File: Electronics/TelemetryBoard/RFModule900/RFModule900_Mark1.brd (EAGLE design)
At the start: 100 x 80 mm, 82 parts, among them U1 TPS2561, U2 TPS2561, Y1 30 Mhz

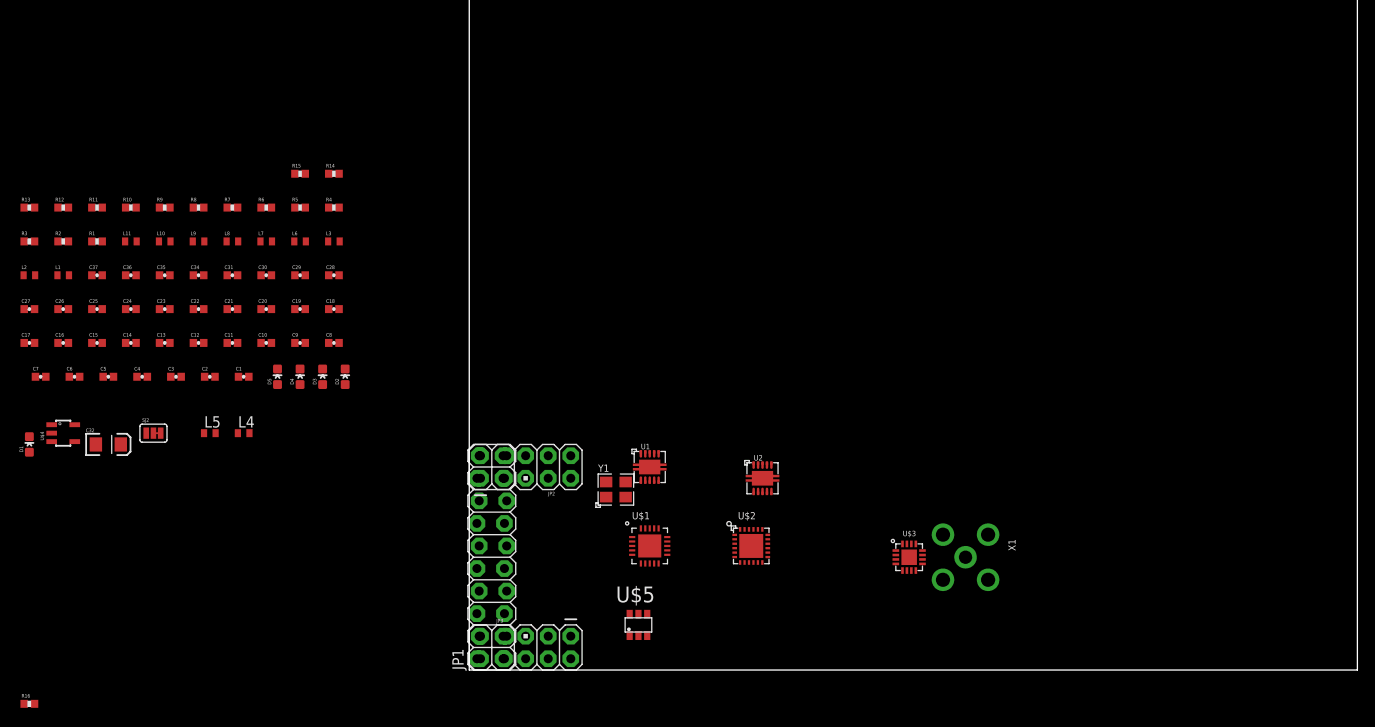
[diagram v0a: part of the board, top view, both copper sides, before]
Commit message: starting board routing
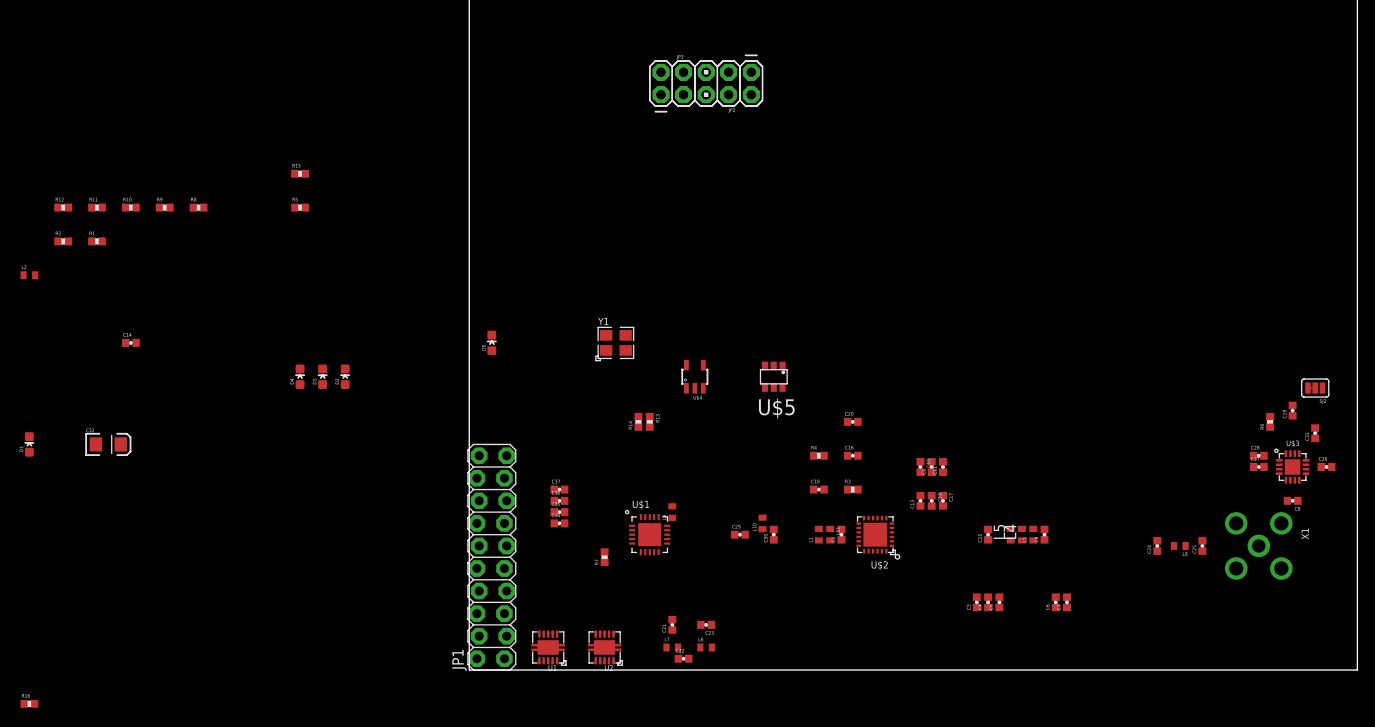
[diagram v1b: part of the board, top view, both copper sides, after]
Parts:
- moved C26 143.3 mm to (96.5, 22.9)
- moved C27 139.6 mm to (88.9, 22.9)
- moved SJ2 130.9 mm to (95.2, 31.8), turned to 180 degrees
- moved C25 127.3 mm to (82.5, 14.0), turned to 90 degrees
- moved C31 123.2 mm to (95.2, 26.7), turned to 90 degrees
- moved C24 118.6 mm to (77.5, 14.0), turned to 90 degrees
- moved C7 118.3 mm to (67.3, 7.62), turned to 90 degrees
- moved R6 115.6 mm to (90.2, 27.9), turned to 90 degrees
- moved C6 113.4 mm to (66.0, 7.62), turned to 90 degrees
- moved C19 112.3 mm to (92.7, 29.2), turned to 90 degrees
- moved L8 112.1 mm to (80.0, 14.0), turned to 180 degrees
- moved C8 109.4 mm to (92.7, 19.1), turned to 180 degrees
- moved C28 106.1 mm to (88.9, 24.1)
- moved C17 104.4 mm to (53.3, 19.1), turned to 270 degrees
- moved C5 103.5 mm to (59.7, 7.62), turned to 90 degrees
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
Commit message: More work on RF card
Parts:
- added C33: 0.01uF, SparkFun-Capacitors:0402-CAP
- C11, C15, C17: device SparkFun-Capacitors:0402-CAP -> SparkFun-Capacitors:EIA3216
- L4, L5: value (none) -> 260; device inductors:0402 -> SparkFun-Passives:0603
- moved L4 115.8 mm to (-49.5, -15.2), turned to 0 degrees
- moved L5 115.7 mm to (-49.5, -19.1), turned to 0 degrees
- moved C15 114.9 mm to (-47.0, -30.5), turned to 0 degrees
- moved C11 110.3 mm to (-47.0, -22.9), turned to 0 degrees
- moved C17 110.3 mm to (-47.0, -26.7), turned to 0 degrees
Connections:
- net GND: now also C11.C, C15.C, C17.C, C33.1; no longer C11.2, C15.2, C17.2
- net N$19: now also C11.A; no longer C11.1
- net N$3: now also C17.A; no longer C17.1
- net N$6: now also L4.2, L5.2; no longer L4.1, L5.1
- net PA_3V3: now also C15.A, C33.2, L4.1, L5.1; no longer C15.1, L4.2, L5.2

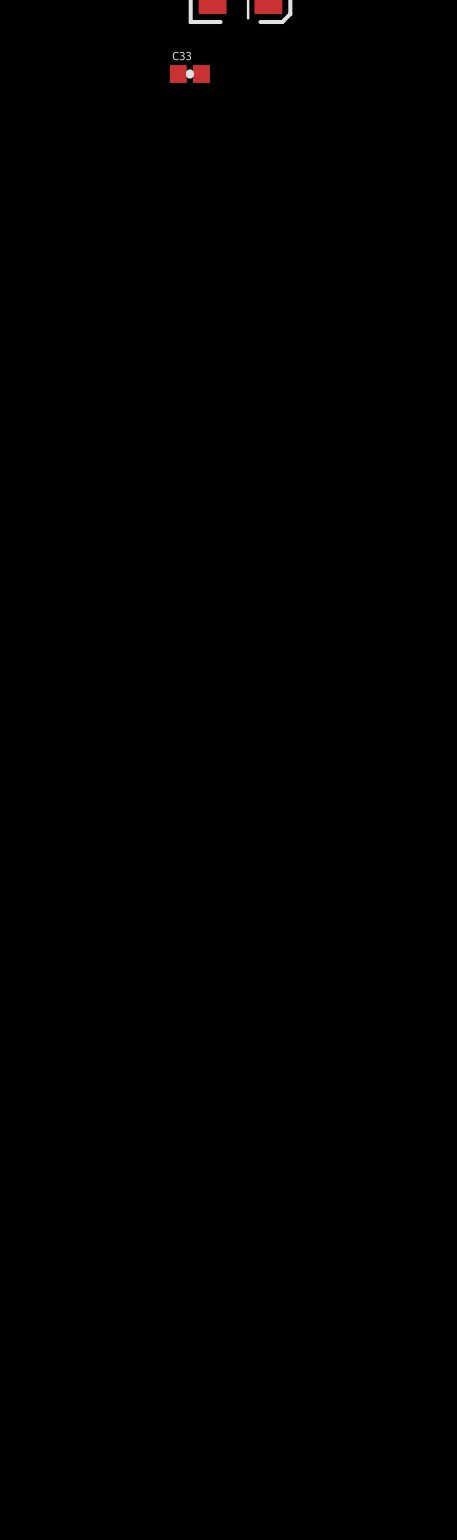
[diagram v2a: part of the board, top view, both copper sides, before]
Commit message: adding directional couplers to board
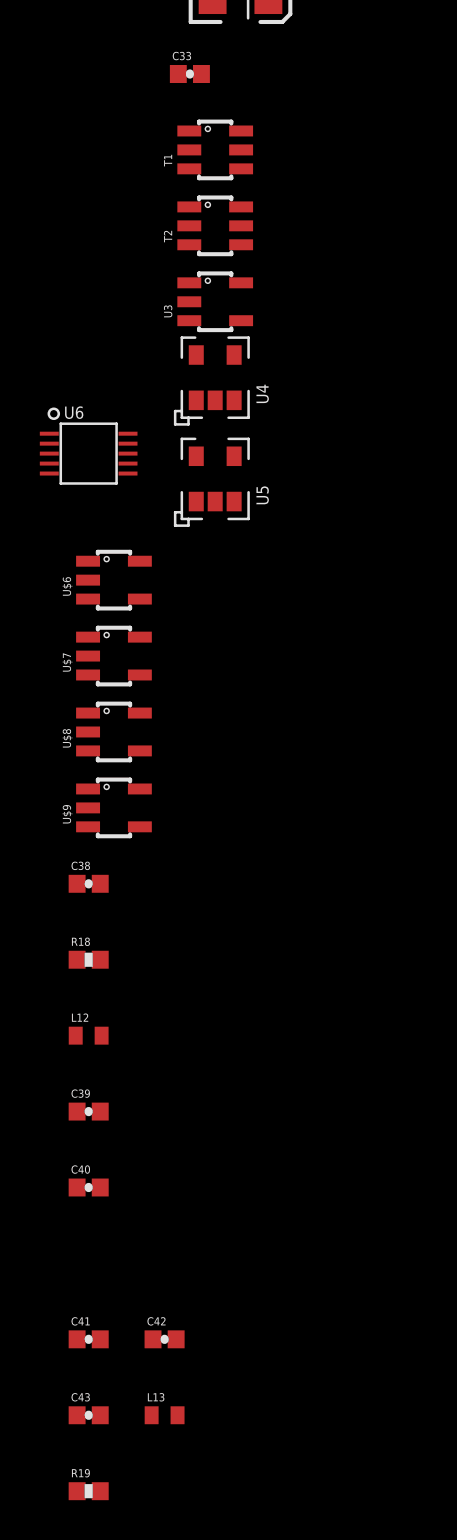
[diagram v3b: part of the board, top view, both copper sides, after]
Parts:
- added C38, C41: 0.1uF, SparkFun-Capacitors:0402-CAP
- added C39, C40, C42, C43: DNP, SparkFun-Capacitors:0402-CAP
- added L12, L13: 0 ohm, SparkFun-Passives:C0402
- added R18, R19: 5k, SparkFun-Resistors:0402-RES
- added T1, T2: DC08-73, RitLaunchInitiative:SOT23-6
- added U$6: TL331-Q1, RitLaunchInitiative:SOT23-5
- added U$7: SN74AHC1G08, RitLaunchInitiative:SOT23-5
- added U$8: SN74LVC1G14, RitLaunchInitiative:SOT23-5
- added U$9: SN74LVC1G32, RitLaunchInitiative:SOT23-5
- added U3: LMV321, RitLaunchInitiative:SOT23-5
- added U4, U5: LTC5505, RitLaunchInitiative:TSOT-23-5
- added U6: MCP4728, RitLaunchInitiative:10-MSOP
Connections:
- new net N$37: R18.1, U4.P$3
- new net N$38: U$8.4, U$9.1
- new net N$39: C40.2, L12.1, T1.3
- new net N$40: C39.2, L12.2, U4.P$1
- new net N$41: T1.6, T2.6
- new net N$42: R19.1
- new net N$43: C43.2, L13.1, U5.P$1
- new net N$44: C42.2, L13.2, T2.3
- new net N$45: T2.4, X1.ANTENNA
- new net N$46: U$7.1, U$9.4
- new net N$47: U$7.2
- new net RF_POWER_IN: U5.P$4
- new net RF_POWER_OUT: U4.P$4
- net 3.3V: now also C38.1, C41.1, R18.2, R19.2, U$6.2, U$8.3, U$9.3, U4.P$5
- net GND: now also C38.2, C39.1, C40.1, C41.2, C42.1, C43.1, T1.1, T1.2, T1.5, T2.1, T2.2, T2.5, U$6.5, U$7.5, U$8.5, U$9.5, U4.P$2
- net N$15: no longer X1.ANTENNA

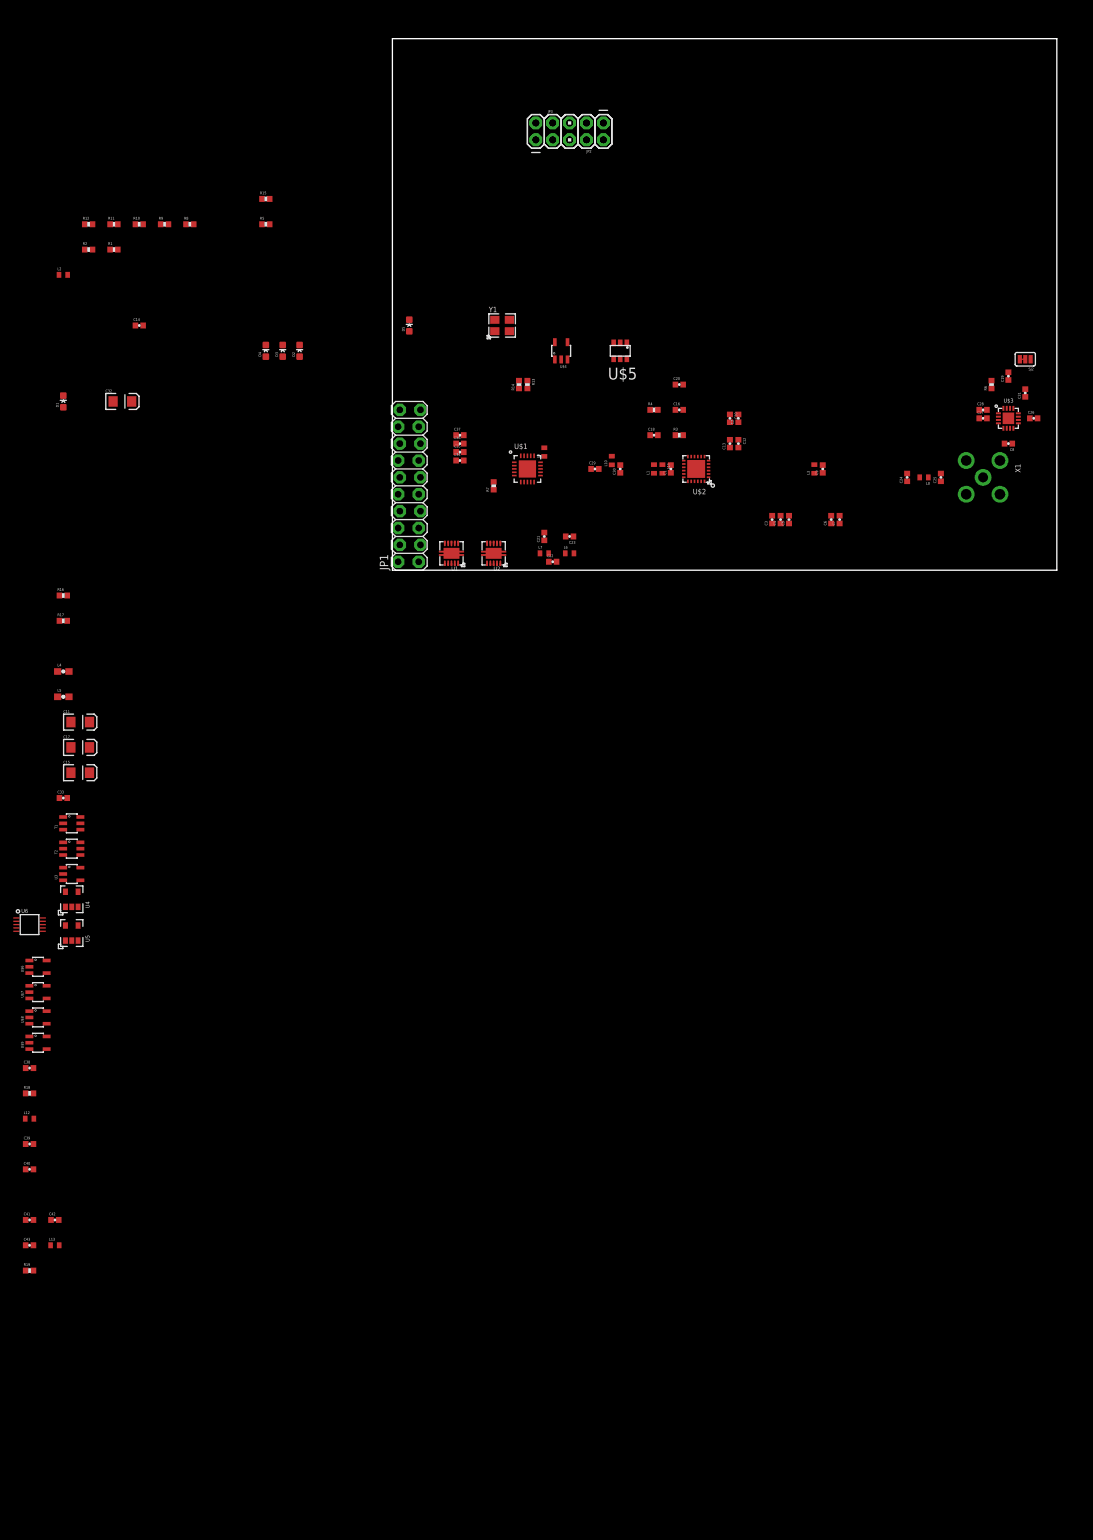
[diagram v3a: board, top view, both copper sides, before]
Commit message: Routing RF path
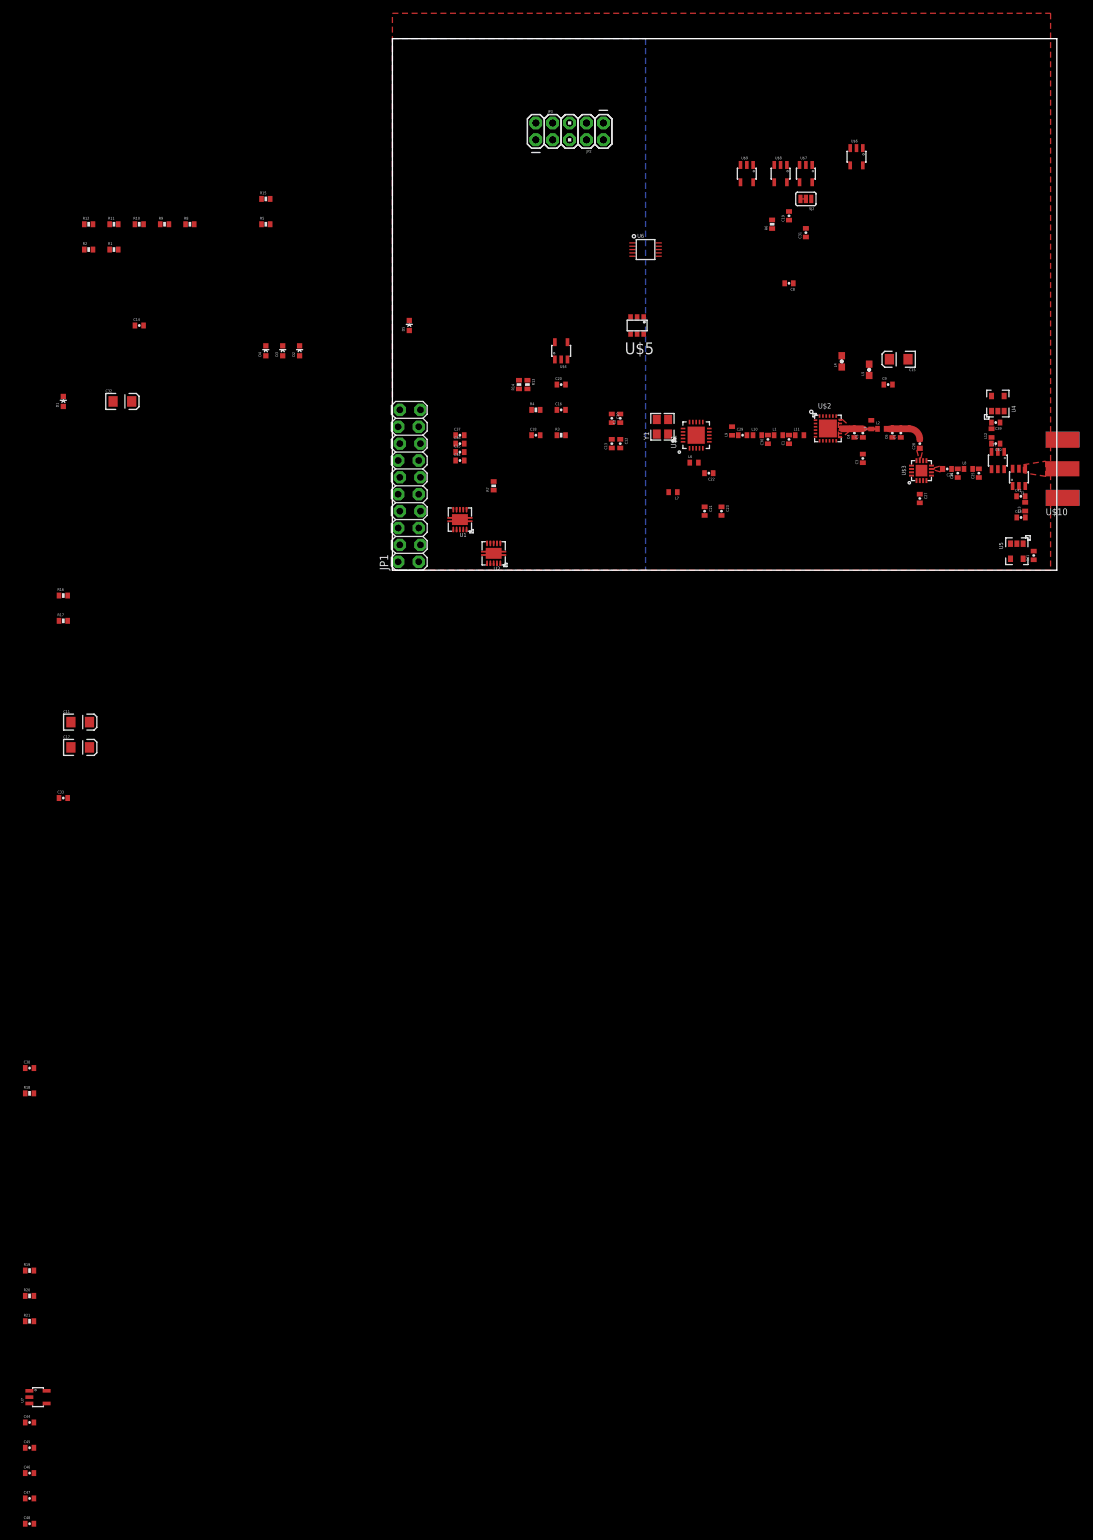
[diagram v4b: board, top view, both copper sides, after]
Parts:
- removed U3: LMV321, RitLaunchInitiative:SOT23-5
- removed X1: (no value), adafruit:SMA90_DIP
- added C44, C45, C46, C47, C48: 0.1uF, SparkFun-Capacitors:0402-CAP
- added R20, R21: 5k, SparkFun-Resistors:0402-RES
- added U$10: 0732511150_SMA_EDGE_LAUNCH, RitLaunchInitiative:SMA_EDGE_LAUNCH
- added U7: LMV321, RitLaunchInitiative:SOT23-5
- JP1: value (none) -> M10X2SPECIAL
- JP2, JP3: value (none) -> M05X2PTH
- moved C43 185.1 mm to (94.6, 7.94)
- moved L13 183.5 mm to (95.2, 9.56), turned to 90 degrees
- moved C40 181.9 mm to (90.8, 19.1), turned to 180 degrees
- moved C42 181.7 mm to (94.6, 11.1)
- moved C39 181.5 mm to (90.8, 22.2), turned to 180 degrees
- moved C41 181.2 mm to (96.5, 2.22), turned to 90 degrees
- moved L12 177.8 mm to (90.2, 20.6), turned to 90 degrees
- moved U$6 173.3 mm to (69.8, 62.2), turned to 270 degrees
- moved U$8 169.2 mm to (58.4, 59.7), turned to 270 degrees
- moved U$7 168.9 mm to (62.2, 59.7), turned to 270 degrees
- moved U$9 168.8 mm to (53.3, 59.7), turned to 270 degrees
- moved U4 158.1 mm to (91.1, 25.1)
- moved U5 153.4 mm to (94.0, 2.86), turned to 180 degrees
- moved T2 153.1 mm to (94.3, 14.0), turned to 90 degrees
- moved T1 149.7 mm to (91.1, 16.5), turned to 270 degrees
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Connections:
- new net N$48: R20.1, R21.2, U7.3
- new net N$51: U$6.4, U$8.2
- new net PA_LOADSWITCH_ENABLE: U$4.3, U$7.4, U2.P$4, U2.P$5
- new net PA_OVERRIDE: U$9.2
- new net REFLECTED_POWER_REF: U$6.1
- net 3.3V: now also C44.2, C45.2, C46.2, C47.2, C48.1, U$7.3, U5.P$5, U7.2
- net GND: now also C44.1, C45.1, C46.1, C47.1, C48.2, R21.1, U$10.GND@1, U$10.GND@2, U$10.GND@3, U$10.GND@5, U5.P$2, U7.5; no longer X1.GND1, X1.GND2, X1.GND3, X1.GND4
- net N$14: now also C27.2; no longer C28.2
- net N$15: now also T1.4
- net N$42: now also U5.P$3
- net N$45: now also U$10.P; no longer X1.ANTENNA
- net N$47: now also R20.2, U$6.3, U7.4; no longer U$7.2
- net N$5: now also C28.2; no longer C27.2
- net PA_ENABLE: now also U$7.2; no longer U$4.3, U2.P$4, U2.P$5
- net RF_POWER_IN: now also U7.1
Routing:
- net N$8: track 0.00 -> 5.74 mm
- net N$5: track 0.00 -> 5.74 mm
- added copper zone on layer 1, net GND
- added copper zone on layer 16, net GND
- added copper zone on layer 1, net N$16
- added copper zone on layer 1, net N$24
- added copper zone on layer 1, net N$45
- added copper zone on layer 1, net N$8

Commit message: wiring in dac
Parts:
- added C49, C50: 10uF, SparkFun-Capacitors:EIA3216
- added SJ1, SJ3, SJ4: (no value), SparkFun-Passives:PAD-JUMPER-3-2OF3_NC_BY_TRACE_YES_SILK_LARGE
- C11: value 10uF -> 0.1uF; device SparkFun-Capacitors:EIA3216 -> SparkFun-Capacitors:0402-CAP
- C17: value 10uF -> 2.2uF; device SparkFun-Capacitors:EIA3216 -> SparkFun-Capacitors:0402-CAP
- moved C11 151.9 mm to (-62.2, -174.0)
- moved C17 151.9 mm to (-62.2, -177.8)
- moved C44 53.9 mm to (-62.2, -181.6)
- moved C46 53.9 mm to (-62.2, -189.2)
- moved C47 53.9 mm to (-62.2, -193.0)
- moved C48 53.9 mm to (-62.2, -196.8)
- moved C45 53.9 mm to (-62.2, -185.4)
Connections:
- net N$18 renamed PA_PWR_REF
- net N$4 renamed PA_PWR_SENSE
- removed net 3V3_MAIN: R13.2
- removed net N$3: C12.1, C17.A, R2.1
- new net N$4: C12.1, C50.A, R2.1, SJ3.2
- new net N$49: C11.1, C17.2, SJ4.2, U6.P$1
- new net SCL: U6.P$2
- new net SDA: U6.P$3
- new net VREG1_DAC: SJ1.3, U6.P$7
- new net VREG2_DAC: SJ3.3, U6.P$8
- net 3.3V: now also C44.1, C45.1, C46.1, C47.1, R13.2, SJ4.3, U$6.5, U$7.5, U$8.5, U$9.5, U7.5; no longer C44.2, C45.2, C46.2, C47.2, U$6.2, U$7.3, U$8.3, U$9.3, U7.2
- net 3V1: now also SJ1.1, SJ3.1
- net 5V: now also SJ4.1
- net GND: now also C11.2, C17.1, C44.2, C45.2, C46.2, C47.2, C49.C, C50.C, U$6.2, U$7.3, U$8.3, U$9.3, U6.P$10, U6.P$4, U7.2; no longer C11.C, C17.C, C44.1, C45.1, C46.1, C47.1, U$6.5, U$7.5, U$8.5, U$9.5, U7.5
- net N$19: now also C49.A, SJ1.2; no longer C11.A
- net REFLECTED_POWER_REF: now also U6.P$6
